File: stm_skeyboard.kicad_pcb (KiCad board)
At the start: 2 copper layers, 51 parts, among them J1 USB4085-GF-A, J2 Conn_01x04_Pin, J3 Conn_01x04_Pin, SW1 SW_Push, SW10 SW_Push, SW11 SW_Push, SW12 SW_Push, SW13 SW_Push, SW14 SW_Push, SW15 SW_Push, SW16 SW_Push, SW2 SW_Push, SW3 SW_Push, SW4 SW_Push, SW5 SW_Push, SW6 SW_Push, SW7 SW_Push, SW8 SW_Push, SW9 SW_Push, U1 TPS7B8133DRVR, U2 STM32L053C8T6

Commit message: switched to bigger matrix, adjusted mcu pins, started pcb layout
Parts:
- removed J2: Conn_01x04_Pin, Connector_PinHeader_2.54mm:PinHeader_1x04_P2.54mm_Vertical
- added D10: D, Diode_SMD:D_0805_2012Metric, F.Cu at (266.5, 111.6)
- added D16: D, Diode_SMD:D_0805_2012Metric, F.Cu at (190.2, 90.7)
- added D17: D, Diode_SMD:D_0805_2012Metric, F.Cu at (209.3, 90.7)
- added D18: D, Diode_SMD:D_0805_2012Metric, F.Cu at (228.4, 90.7)
- added D19: D, Diode_SMD:D_0805_2012Metric, F.Cu at (247.4, 90.7)
- added D20: D, Diode_SMD:D_0805_2012Metric, F.Cu at (266.5, 90.7)
- added D26: D, Diode_SMD:D_0805_2012Metric, F.Cu at (190.2, 76.2)
- added D27: D, Diode_SMD:D_0805_2012Metric, F.Cu at (209.3, 76.2)
- added D28: D, Diode_SMD:D_0805_2012Metric, F.Cu at (228.4, 76.2)
- added D29: D, Diode_SMD:D_0805_2012Metric, F.Cu at (247.4, 76.2)
- added D30: D, Diode_SMD:D_0805_2012Metric, F.Cu at (266.5, 76.2)
- added D6: D, Diode_SMD:D_0805_2012Metric, F.Cu at (190.0, 111.6)
- added D7: D, Diode_SMD:D_0805_2012Metric, F.Cu at (209.1, 111.6)
- added D8: D, Diode_SMD:D_0805_2012Metric, F.Cu at (228.2, 111.6)
- added D9: D, Diode_SMD:D_0805_2012Metric, F.Cu at (247.3, 111.6)
- added SW10: SW_Push, Button_Switch_Keyboard:SW_Cherry_MX_1.00u_PCB, F.Cu at (266.5, 118.3)
- added SW16: SW_Push, Button_Switch_Keyboard:SW_Cherry_MX_1.00u_PCB, F.Cu at (190.3, 137.4)
- added SW17: SW_Push, Button_Switch_Keyboard:SW_Cherry_MX_1.00u_PCB, F.Cu at (209.3, 137.4)
- added SW18: SW_Push, Button_Switch_Keyboard:SW_Cherry_MX_1.00u_PCB, F.Cu at (228.4, 137.4)
- added SW19: SW_Push, Button_Switch_Keyboard:SW_Cherry_MX_1.00u_PCB, F.Cu at (247.4, 137.4)
- added SW20: SW_Push, Button_Switch_Keyboard:SW_Cherry_MX_1.00u_PCB, F.Cu at (266.5, 137.4)
- added SW26: SW_Push, Button_Switch_Keyboard:SW_Cherry_MX_1.00u_PCB, F.Cu at (190.3, 156.4)
- added SW27: SW_Push, Button_Switch_Keyboard:SW_Cherry_MX_1.00u_PCB, F.Cu at (209.3, 156.4)
- added SW28: SW_Push, Button_Switch_Keyboard:SW_Cherry_MX_1.00u_PCB, F.Cu at (228.4, 156.4)
- added SW29: SW_Push, Button_Switch_Keyboard:SW_Cherry_MX_1.00u_PCB, F.Cu at (247.4, 156.4)
- added SW30: SW_Push, Button_Switch_Keyboard:SW_Cherry_MX_1.00u_PCB, F.Cu at (266.5, 156.4)
- added SW6: SW_Push, Button_Switch_Keyboard:SW_Cherry_MX_1.00u_PCB, F.Cu at (190.3, 118.3)
- added SW7: SW_Push, Button_Switch_Keyboard:SW_Cherry_MX_1.00u_PCB, F.Cu at (209.3, 118.3)
- added SW8: SW_Push, Button_Switch_Keyboard:SW_Cherry_MX_1.00u_PCB, F.Cu at (228.4, 118.3)
- added SW9: SW_Push, Button_Switch_Keyboard:SW_Cherry_MX_1.00u_PCB, F.Cu at (247.4, 118.3)
- moved D21 131.7 mm to (95.0, 76.2), turned to -90 degrees
- moved D1 128.6 mm to (95.0, 111.6), turned to -90 degrees
- moved D11 126.0 mm to (95.0, 90.7), turned to -90 degrees
- moved D22 113.5 mm to (114.0, 76.2), turned to -90 degrees
- moved D12 111.2 mm to (114.0, 90.7), turned to -90 degrees
- moved D2 109.2 mm to (114.1, 111.6), turned to -90 degrees
- moved SW12 98.5 mm to (114.1, 137.4)
- moved SW14 98.5 mm to (152.2, 137.4)
- moved SW15 98.5 mm to (171.2, 137.4)
- moved SW2 98.5 mm to (114.1, 118.3)
- moved SW22 98.5 mm to (114.1, 156.4)
- moved SW24 98.5 mm to (152.2, 156.4)
- moved SW25 98.5 mm to (171.2, 156.4)
- moved SW4 98.5 mm to (152.2, 118.3)
- moved SW5 98.5 mm to (171.2, 118.3)
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- renumbered D6 to D11, D7 to D12, D8 to D13, D9 to D14, D10 to D15, D11 to D21, D12 to D22, D13 to D23, D14 to D24, D15 to D25, SW6 to SW11, SW7 to SW12, SW8 to SW13, SW9 to SW14, SW10 to SW15, SW11 to SW21, SW12 to SW22, SW13 to SW23, SW14 to SW24, SW15 to SW25, SW16 to SW31
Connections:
- net Net-(R3-Pad1) renamed /mcu/boot0
- net Net-(U2-NRST) renamed /mcu/NRST
- C8 pad 2: unconnected-(C8-Pad2) -> GND
- U2 pad 12: /mcu/UART2_TX -> unconnected-(U2-PA2-Pad12)
- U2 pad 13: /mcu/UART2_TX -> /matrix/COL0
- U2 pad 14: unconnected-(U2-PA4-Pad14) -> /matrix/COL1
- U2 pad 15: unconnected-(U2-PA5-Pad15) -> /matrix/COL2
- U2 pad 16: unconnected-(U2-PA6-Pad16) -> /matrix/COL3
- U2 pad 17: unconnected-(U2-PA7-Pad17) -> /matrix/COL4
- U2 pad 21: /matrix/ROW2 -> unconnected-(U2-PB10-Pad21)
- U2 pad 22: /matrix/COL0 -> unconnected-(U2-PB11-Pad22)
- U2 pad 25: /matrix/COL1 -> /matrix/COL9
- U2 pad 26: /matrix/COL2 -> /matrix/COL8
- U2 pad 27: /matrix/COL3 -> /matrix/COL7
- U2 pad 28: /matrix/COL4 -> /matrix/COL6
- U2 pad 29: unconnected-(U2-PA8-Pad29) -> /matrix/COL5
- U2 pad 40: unconnected-(U2-PB4-Pad40) -> /matrix/ROW2
- U2 pad 41: unconnected-(U2-PB5-Pad41) -> /matrix/ROW1
- U2 pad 42: unconnected-(U2-PB6-Pad42) -> /matrix/ROW0
- U2 pad 45: /matrix/ROW0 -> unconnected-(U2-PB8-Pad45)
- U2 pad 46: /matrix/ROW1 -> unconnected-(U2-PB9-Pad46)

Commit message: added 3d models, completed 0.1
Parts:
- added H1: MountingHole, MountingHole:MountingHole_2.1mm, F.Cu at (66.0, 86.5)
- added H2: MountingHole, MountingHole:MountingHole_2.1mm, F.Cu at (261.0, 86.5)
- added H3: MountingHole, MountingHole:MountingHole_2.1mm, F.Cu at (66.0, 155.5)
- added H4: MountingHole, MountingHole:MountingHole_2.1mm, F.Cu at (261.0, 155.5)
- SW1, SW10, SW11, SW12, SW13, SW14, SW15, SW16, SW17, SW18, SW19, SW2, SW20, SW21, SW22, SW23, SW24, SW25, SW26, SW27, SW28, SW29, SW3, SW30, SW4, SW5, SW6, SW7, SW8, SW9: footprint Button_Switch_Keyboard:SW_Cherry_MX_1.00u_PCB -> my_switch:SW_Cherry_MX_1.00u_PCB
- moved C5 113.4 mm to (147.4, 97.8), turned to 90 degrees
- moved C8 105.5 mm to (150.1, 88.7), turned to 90 degrees
- moved C12 103.7 mm to (135.5, 91.1)
- moved C10 103.7 mm to (136.0, 88.7)
- moved C11 103.7 mm to (134.6, 88.7)
- moved C3 103.7 mm to (144.7, 98.6)
- moved C6 103.7 mm to (135.7, 93.1)
- moved C7 103.7 mm to (134.2, 93.1)
- moved U2 103.7 mm to (142.2, 92.0)
- moved C4 103.6 mm to (139.7, 86.0), turned to 0 degrees
- moved C9 102.7 mm to (148.6, 88.7), turned to 90 degrees
- moved J3 74.1 mm to (123.2, 95.6)
- moved C1 72.1 mm to (168.5, 98.0), turned to 0 degrees
- moved R3 71.8 mm to (110.6, 91.8), turned to 180 degrees
- moved J1 67.3 mm to (166.6, 92.8)
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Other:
- board outline added: 201 x 75 mm
- board text added: "BOOT"

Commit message: added routing
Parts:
- D1, D10, D11, D12, D13, D14, D15, D16, D17, D18, D19, D2, D20, D21, D22, D23, D24, D25, D26, D27, D28, D29, D3, D30, D4, D5, D6, D7, D8, D9: footprint Diode_SMD:D_0805_2012Metric -> Diode_SMD:D_SOD-523
- R2: moved to B.Cu
- moved D4 12.4 mm to (125.7, 103.1), turned to 0 degrees
- moved J3 9.80 mm to (123.5, 85.8), turned to -90 degrees
- moved R2 5.95 mm to (162.3, 89.1), turned to 90 degrees
- moved SW31 1.91 mm to (106.0, 92.7), turned to 90 degrees
- moved D5 0.86 mm to (156.7, 98.7)
- moved R1 0.60 mm to (165.5, 94.9)
- moved C12 0.30 mm to (135.4, 90.8)
- moved J1 0.20 mm to (166.6, 92.6)
- turned R3 to 0 degrees
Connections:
- U2 pad 25: /matrix/COL9 -> /matrix/COL5
- U2 pad 26: /matrix/COL8 -> /matrix/COL6
- U2 pad 28: /matrix/COL6 -> /matrix/COL8
- U2 pad 29: /matrix/COL5 -> /matrix/COL9
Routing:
- net /matrix/ROW2: track 0.00 -> 305.7 mm, vias 0 -> 4
- net /matrix/ROW1: track 0.00 -> 205.7 mm, vias 0 -> 2
- net /matrix/ROW0: track 0.00 -> 189.1 mm, vias 0 -> 6
- net /matrix/COL9: track 0.00 -> 153.3 mm, vias 0 -> 8
- net /matrix/COL8: track 0.00 -> 140.9 mm, vias 0 -> 8
- net +3.3V: track 0.00 -> 131.8 mm
- net /matrix/COL0: track 0.00 -> 108.7 mm, vias 0 -> 1
- net /matrix/COL7: track 0.00 -> 104.1 mm, vias 0 -> 5
- net /matrix/COL6: track 0.00 -> 90.5 mm, vias 0 -> 5
- net /matrix/COL1: track 0.00 -> 90.4 mm, vias 0 -> 5
- net /matrix/COL2: track 0.00 -> 72.1 mm, vias 0 -> 5
- net /matrix/COL5: track 0.00 -> 69.3 mm, vias 0 -> 6
- net /matrix/COL4: track 0.00 -> 61.6 mm, vias 0 -> 8
- net /matrix/COL3: track 0.00 -> 56.6 mm, vias 0 -> 5
- net /mcu/SWDIO: track 0.00 -> 40.7 mm, vias 0 -> 3
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- added copper zone on B.Cu, net GND

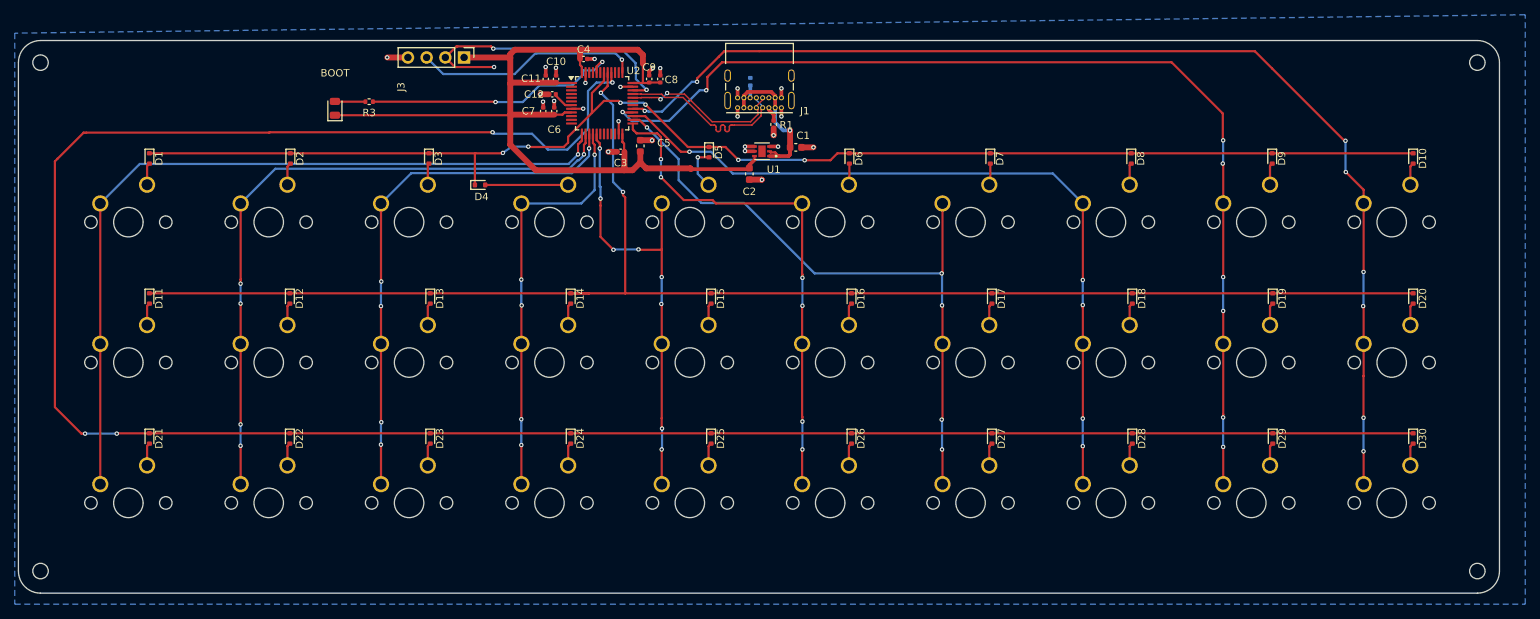
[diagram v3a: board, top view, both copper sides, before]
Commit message: repair decoupling and fill front layer
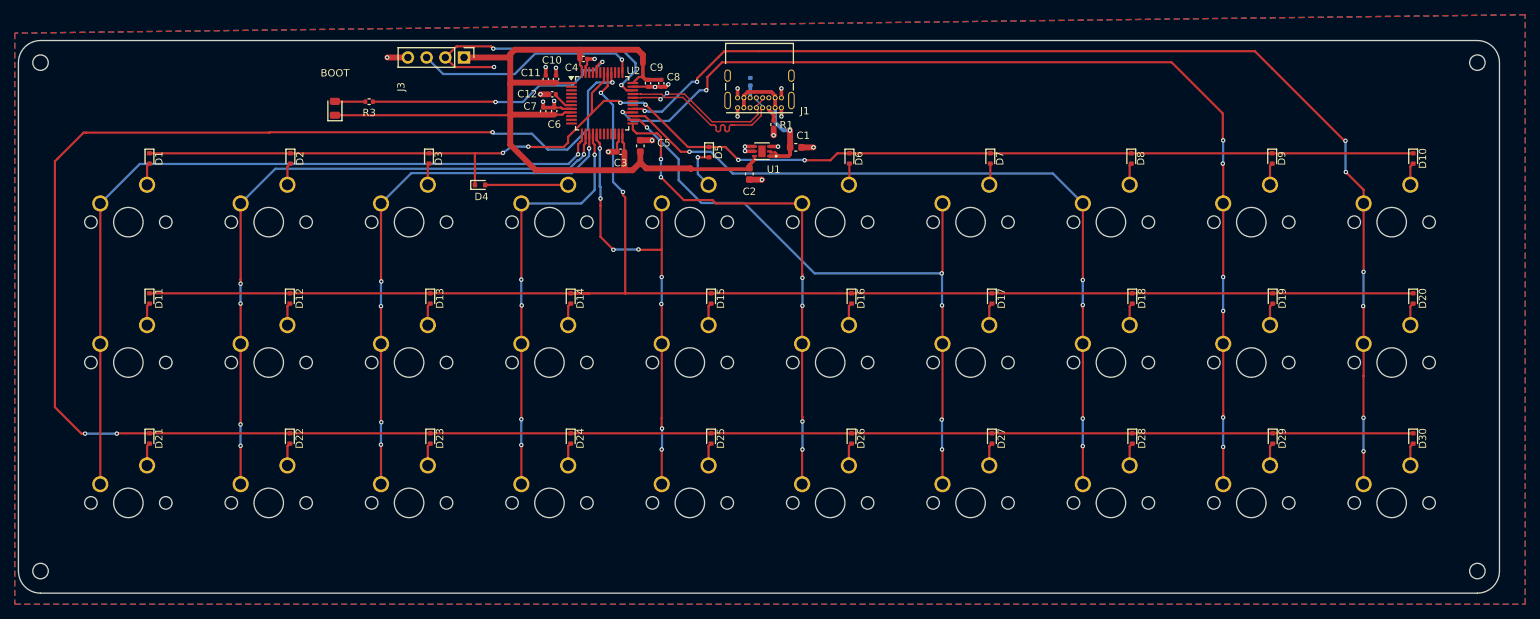
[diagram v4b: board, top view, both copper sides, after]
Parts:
- moved C9 0.60 mm to (148.4, 89.3), turned to -90 degrees
- moved C8 0.60 mm to (150.2, 89.3), turned to -90 degrees
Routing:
- net GND: track 33.3 -> 38.0 mm, vias 25 -> 21
- net /mcu/SWDIO: track 40.7 -> 40.2 mm
- added copper zone on F.Cu, net GND

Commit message: re-done whole pcb
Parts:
- removed C10: 100n, Capacitor_SMD:C_0402_1005Metric
- removed C11: 1u, Capacitor_SMD:C_0402_1005Metric
- J1: value USB4085-GF-A -> GSB1C411111DS1HR; footprint Connector_USB:USB_C_Receptacle_GCT_USB4085 -> usb_personal:AMPHENOL_GSB1C411111DS1HR
- R2: moved to F.Cu
- SW1, SW10, SW11, SW12, SW13, SW14, SW15, SW16, SW17, SW18, SW19, SW2, SW20, SW21, SW22, SW23, SW24, SW25, SW26, SW27, SW28, SW29, SW3, SW30, SW4, SW5, SW6, SW7, SW8, SW9: footprint my_switch:SW_Cherry_MX_1.00u_PCB -> my_switch:SW_Cherry_MX_1.00u_PCB_no_support_stems; moved to B.Cu
- moved H4 206.2 mm to (57.2, 124.2)
- moved H3 180.9 mm to (244.2, 124.2)
- moved SW21 62.7 mm to (67.7, 79.8)
- moved SW22 62.7 mm to (86.8, 79.8)
- moved SW23 62.7 mm to (105.8, 79.8)
- moved SW24 62.7 mm to (124.9, 79.8)
- moved SW25 62.7 mm to (143.9, 79.8)
- moved SW26 62.7 mm to (163.0, 79.8)
- moved SW27 62.7 mm to (182.0, 79.8)
- moved SW28 62.7 mm to (201.1, 79.8)
- moved SW29 62.7 mm to (220.1, 79.8)
- moved SW30 62.7 mm to (239.2, 79.8)
- moved D25 55.3 mm to (140.7, 84.6), turned to 90 degrees
- moved D21 54.5 mm to (67.7, 84.6), turned to 90 degrees
- moved D22 54.5 mm to (86.8, 84.6), turned to 90 degrees
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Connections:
- U2 pad 13: /matrix/COL0 -> unconnected-(U2-PA3-Pad13)
- U2 pad 14: /matrix/COL1 -> unconnected-(U2-PA4-Pad14)
- U2 pad 15: /matrix/COL2 -> unconnected-(U2-PA5-Pad15)
- U2 pad 16: /matrix/COL3 -> /matrix/ROW0
- U2 pad 17: /matrix/COL4 -> /matrix/ROW1
- U2 pad 2: unconnected-(U2-PC13-Pad2) -> /matrix/COL0
- U2 pad 25: /matrix/COL5 -> /matrix/COL6
- U2 pad 26: /matrix/COL6 -> /matrix/COL5
- U2 pad 3: unconnected-(U2-PC14-Pad3) -> /matrix/COL4
- U2 pad 38: unconnected-(U2-PA15-Pad38) -> /matrix/ROW2
- U2 pad 4: unconnected-(U2-PC15-Pad4) -> /matrix/COL3
- U2 pad 40: /matrix/ROW2 -> unconnected-(U2-PB4-Pad40)
- U2 pad 41: /matrix/ROW1 -> /matrix/COL2
- U2 pad 42: /matrix/ROW0 -> /matrix/COL1
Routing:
- net /matrix/ROW2: track 305.7 -> 176.4 mm, vias 4 -> 2
- net /matrix/COL0: track 108.7 -> 148.0 mm, vias 1 -> 2
- net /matrix/COL6: track 90.5 -> 61.6 mm, vias 5 -> 1
- net /matrix/COL8: track 140.9 -> 112.2 mm, vias 8 -> 0
- net /matrix/COL3: track 56.6 -> 83.5 mm, vias 5 -> 3
- net /matrix/COL5: track 69.3 -> 43.5 mm, vias 6 -> 0
- net /matrix/ROW0: track 189.1 -> 213.6 mm, vias 6 -> 4
- net /matrix/COL1: track 90.4 -> 112.6 mm, vias 5 -> 2
- net +3.3V: track 131.7 -> 111.6 mm
- net /matrix/COL9: track 153.3 -> 134.7 mm, vias 8 -> 0
- net /matrix/COL7: track 104.1 -> 89.4 mm, vias 5 -> 0
- net /matrix/COL2: track 72.1 -> 86.8 mm, vias 5 -> 3
- net GND: track 38.0 -> 26.8 mm, vias 21 -> 76
- net /mcu/BOOT0: track 35.6 -> 46.4 mm, vias 2 -> 4
- net /matrix/ROW1: track 205.7 -> 197.6 mm
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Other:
- board size 201 x 75 mm -> 195 x 69 mm

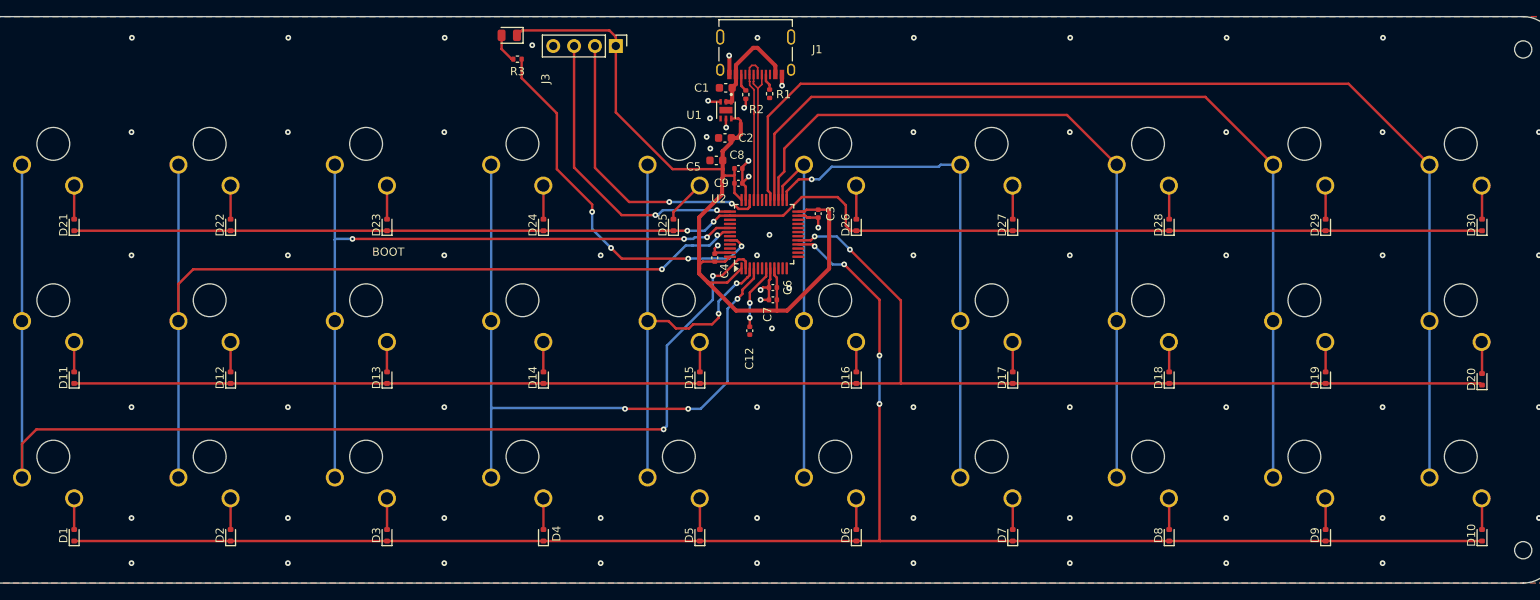
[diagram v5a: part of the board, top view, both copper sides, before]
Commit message: added ESD protection, re-wired matrix
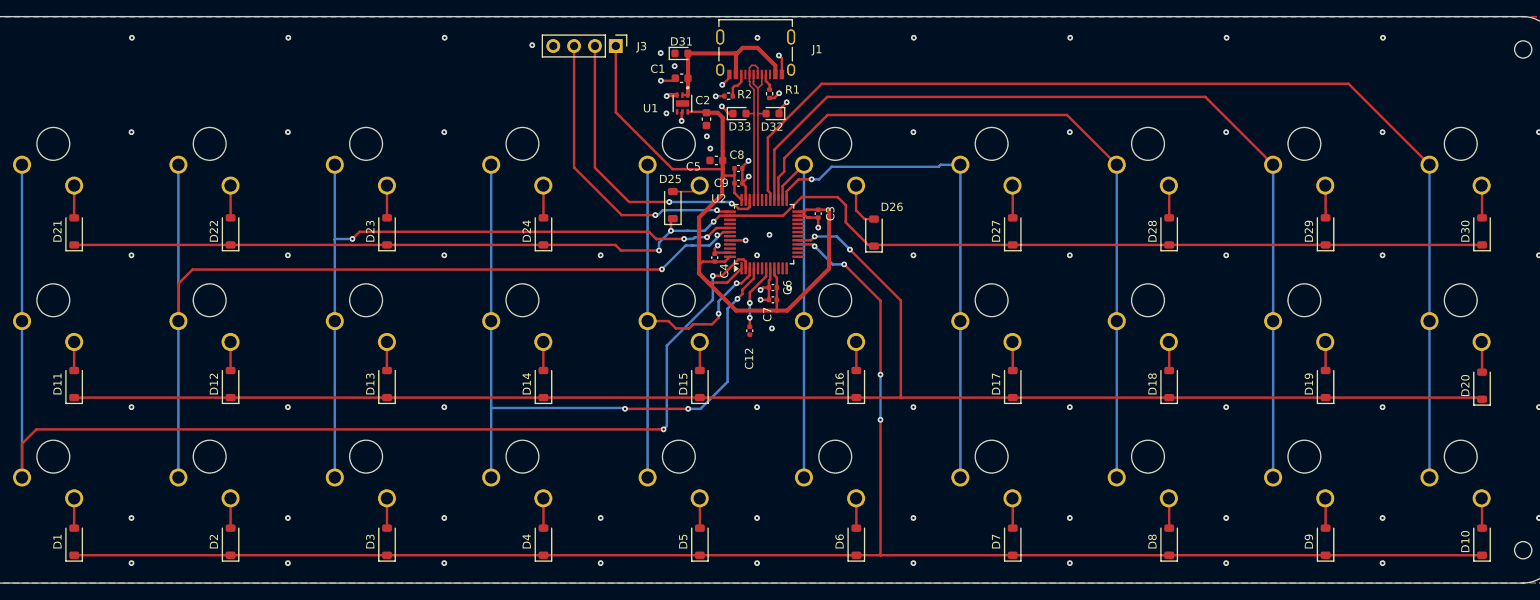
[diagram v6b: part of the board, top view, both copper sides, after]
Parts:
- removed R3: 10k, Resistor_SMD:R_0402_1005Metric
- removed SW31: SW_Push, Diode_SMD:D_0805_2012Metric
- added D31: 82306050029, Diode_SMD:D_0603_1608Metric, F.Cu at (141.7, 63.7)
- added D32: 82306050029, Diode_SMD:D_0603_1608Metric, F.Cu at (152.8, 71.1)
- added D33: 82306050029, Diode_SMD:D_0603_1608Metric, F.Cu at (148.8, 71.1)
- D1, D10, D11, D12, D13, D14, D15, D16, D17, D18, D19, D2, D20, D21, D22, D23, D24, D25, D26, D27, D28, D29, D3, D30, D4, D5, D6, D7, D8, D9: footprint Diode_SMD:D_SOD-523 -> Diode_SMD:D_SOD-123
- moved C1 5.50 mm to (141.7, 66.8)
- moved U1 5.36 mm to (141.8, 69.8)
- moved C2 3.21 mm to (144.7, 71.7), turned to -90 degrees
- moved D25 2.42 mm to (140.6, 82.2)
- moved D26 2.34 mm to (165.1, 85.6)
- moved R2 2.10 mm to (147.4, 68.9), turned to 180 degrees
- moved D11 0.78 mm to (67.7, 104.0)
- moved D12 0.78 mm to (86.8, 104.0)
- moved D13 0.78 mm to (105.8, 104.0)
- moved D14 0.78 mm to (124.9, 104.0)
- moved D15 0.78 mm to (143.9, 104.0)
- moved D16 0.78 mm to (163.0, 104.0)
- moved D17 0.78 mm to (182.0, 104.0)
- moved D18 0.78 mm to (201.1, 104.0)
- moved D19 0.78 mm to (220.2, 104.0)
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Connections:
- U2 pad 44: /mcu/BOOT0 -> GND
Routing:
- net /mcu/BOOT0: track 46.4 -> 0.00 mm, vias 4 -> 0
- net +3.3V: track 111.6 -> 100.1 mm
- net GND: track 26.8 -> 35.6 mm, vias 76 -> 83
- net +5V: track 13.0 -> 21.2 mm
- net /matrix/ROW2: track 176.4 -> 180.2 mm, vias 2 -> 3
- net /mcu/boot0: track 3.60 -> 0.00 mm
- net /matrix/ROW0: track 213.6 -> 215.5 mm
- net Net-(D25-A): track 5.43 -> 3.58 mm
- net /matrix/ROW1: track 197.6 -> 199.3 mm
- net Net-(D26-A): track 4.11 -> 5.68 mm
- net /matrix/COL9: track 134.7 -> 133.2 mm
- net /matrix/COL8: track 112.2 -> 111.1 mm
- net Net-(J1-CC2): track 2.17 -> 3.24 mm
- net /mcu/USB_D-: track 17.4 -> 18.4 mm
- net /mcu/USB_D+: track 18.4 -> 19.4 mm
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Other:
- board text removed: "BOOT"
